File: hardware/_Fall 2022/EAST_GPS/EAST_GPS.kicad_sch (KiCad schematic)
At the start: 3 parts, among them J1 Conn_02x09_Odd_Even, U1 GPS-14414, U2 RFM69HCW_Breakout

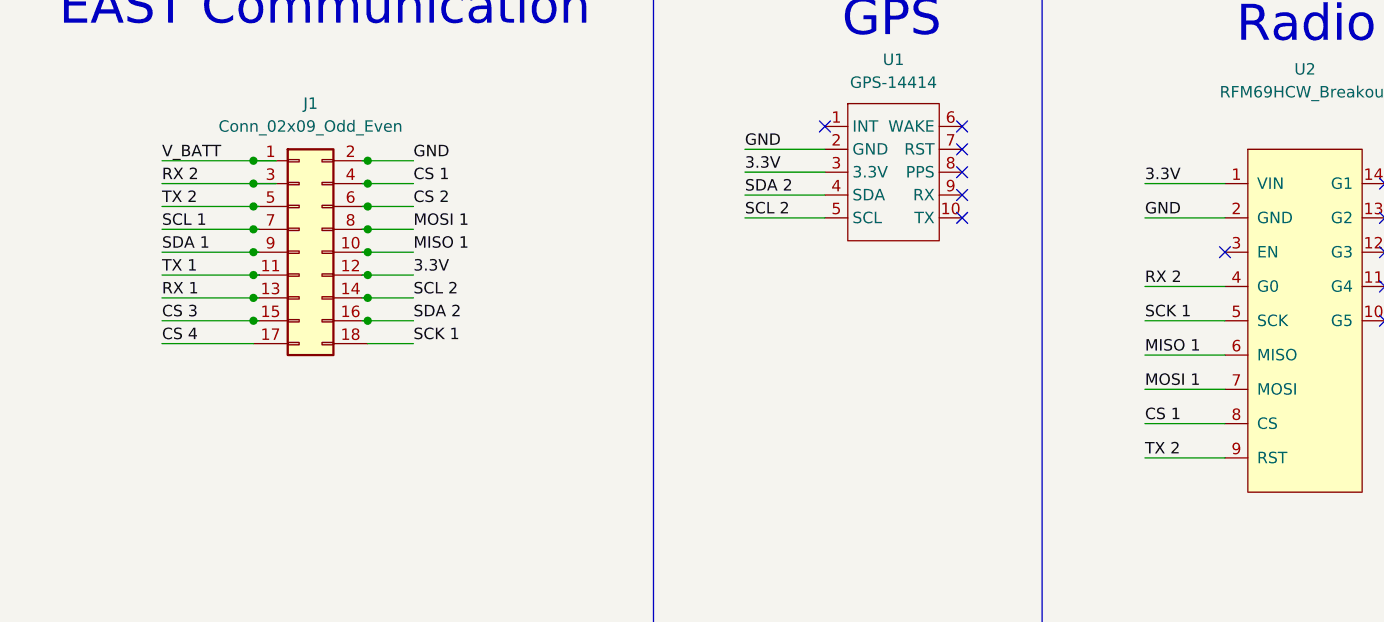
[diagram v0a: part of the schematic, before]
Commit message: fixed a few pcb silkscreen things
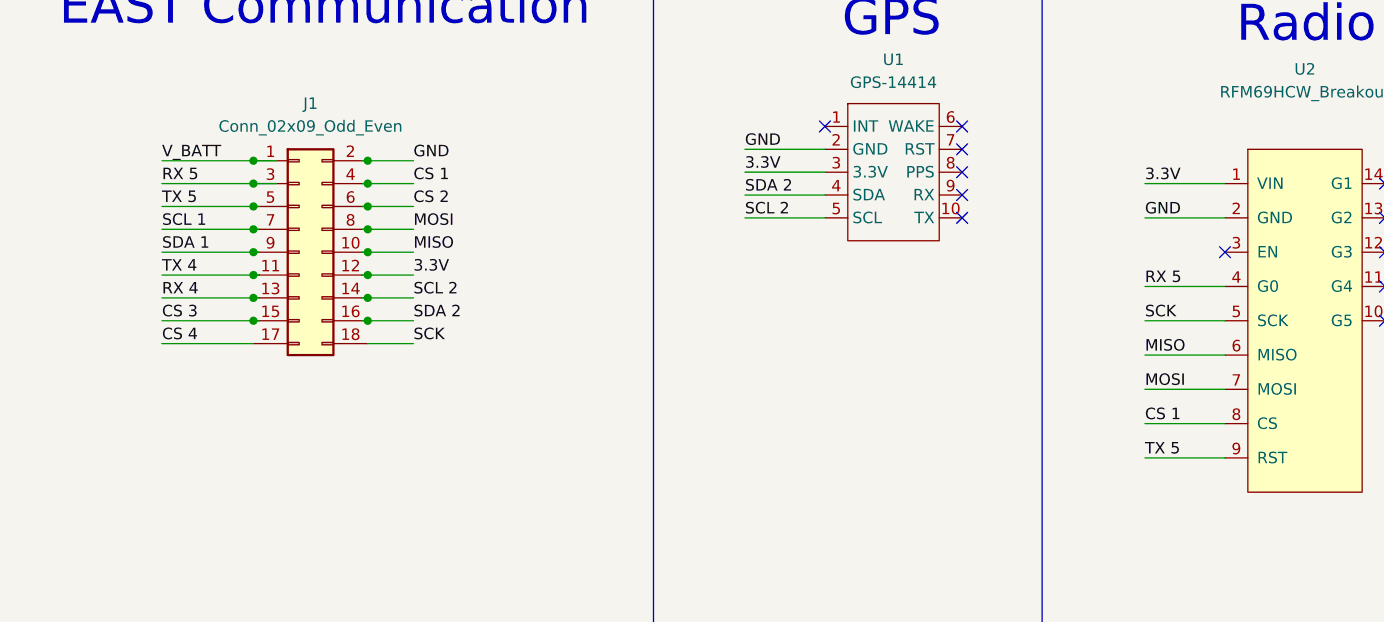
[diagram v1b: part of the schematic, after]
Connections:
- net MISO 1 renamed MISO
- net MOSI 1 renamed MOSI
- net RX 1 renamed RX 4
- net RX 2 renamed RX 5
- net SCK 1 renamed SCK
- net TX 1 renamed TX 4
- net TX 2 renamed TX 5
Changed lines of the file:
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@@
     (effects (font (size 1.27 1.27)) (justify left bottom))
   )
-  (label "MISO 1" (at 62.23 53.34 0)
+  (label "MISO" (at 62.23 53.34 0)
     (effects (font (size 1.27 1.27)) (justify left bottom))
   )
@@
     (effects (font (size 1.27 1.27)) (justify left bottom))
   )
-  (label "TX 2" (at 34.29 48.26 0)
+  (label "TX 5" (at 34.29 48.26 0)
     (effects (font (size 1.27 1.27)) (justify left bottom))
   )
-  (label "MOSI 1" (at 143.51 68.58 0)
+  (label "MOSI" (at 143.51 68.58 0)
     (effects (font (size 1.27 1.27)) (justify left bottom))
   )
@@
     (effects (font (size 1.27 1.27)) (justify left bottom))
   )
-  (label "MISO 1" (at 143.51 64.77 0)
+  (label "MISO" (at 143.51 64.77 0)
     (effects (font (size 1.27 1.27)) (justify left bottom))
   )
@@
     (effects (font (size 1.27 1.27)) (justify left bottom))
   )
-  (label "TX 2" (at 143.51 76.2 0)
+  (label "TX 5" (at 143.51 76.2 0)
     (effects (font (size 1.27 1.27)) (justify left bottom))
   )
@@
     (effects (font (size 1.27 1.27)) (justify left bottom))
   )
-  (label "TX 1" (at 34.29 55.88 0)
+  (label "TX 4" (at 34.29 55.88 0)
     (effects (font (size 1.27 1.27)) (justify left bottom))
   )
-  (label "RX 2" (at 143.51 57.15 0)
+  (label "RX 5" (at 143.51 57.15 0)
     (effects (font (size 1.27 1.27)) (justify left bottom))
   )
@@
     (effects (font (size 1.27 1.27)) (justify left bottom))
   )
-  (label "SCK 1" (at 62.23 63.5 0)
+  (label "SCK" (at 62.23 63.5 0)
     (effects (font (size 1.27 1.27)) (justify left bottom))
   )
@@
     (effects (font (size 1.27 1.27)) (justify left bottom))
   )
-  (label "MOSI 1" (at 62.23 50.8 0)
+  (label "MOSI" (at 62.23 50.8 0)
     (effects (font (size 1.27 1.27)) (justify left bottom))
   )
-  (label "SCK 1" (at 143.51 60.96 0)
+  (label "SCK" (at 143.51 60.96 0)
     (effects (font (size 1.27 1.27)) (justify left bottom))
   )
-  (label "RX 1" (at 34.29 58.42 0)
+  (label "RX 4" (at 34.29 58.42 0)
     (effects (font (size 1.27 1.27)) (justify left bottom))
   )
@@
     (effects (font (size 1.27 1.27)) (justify left bottom))
   )
-  (label "RX 2" (at 34.29 45.72 0)
+  (label "RX 5" (at 34.29 45.72 0)
     (effects (font (size 1.27 1.27)) (justify left bottom))
   )

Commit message: pcb ship version
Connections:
- net SCL 1: now also U1.5 (SCL)
- net SCL 2: no longer U1.5 (SCL)
- net SDA 1: now also U1.4 (SDA)
- net SDA 2: no longer U1.4 (SDA)
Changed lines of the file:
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@@
     (effects (font (size 1.27 1.27)) (justify left bottom))
   )
-  (label "SDA 2" (at 99.06 46.99 0)
+  (label "SDA 1" (at 99.06 46.99 0)
     (effects (font (size 1.27 1.27)) (justify left bottom))
   )
@@
     (effects (font (size 1.27 1.27)) (justify left bottom))
   )
-  (label "SCL 2" (at 99.06 49.53 0)
+  (label "SCL 1" (at 99.06 49.53 0)
     (effects (font (size 1.27 1.27)) (justify left bottom))
   )
